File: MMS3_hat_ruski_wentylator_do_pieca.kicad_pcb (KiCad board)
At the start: 2 copper layers, 100 x 50 mm, 72 parts, among them J1 Chainbus in, J2 Chainbus Out, J3 Conn_01x04_Pin, J4 AMASS XT60 Male, J5 AMASS XT60 Female, J6 Conn_01x04_Socket, J7 Program, J9 Conn_01x06_Socket, Q1 PMOS, Q10 AO3401A, Q11 MMBT5401 200-300, Q12 MMBT5551 200-300, Q9 MMBT5551 200-300, U1 SN74CB3Q3245PWR, U2 M24C64, U3 XL6019E1, U4 AMS1117, U5 CH32V003FxPx, U6 MCP4161-502E/SN, X2 X322525MOB4SI

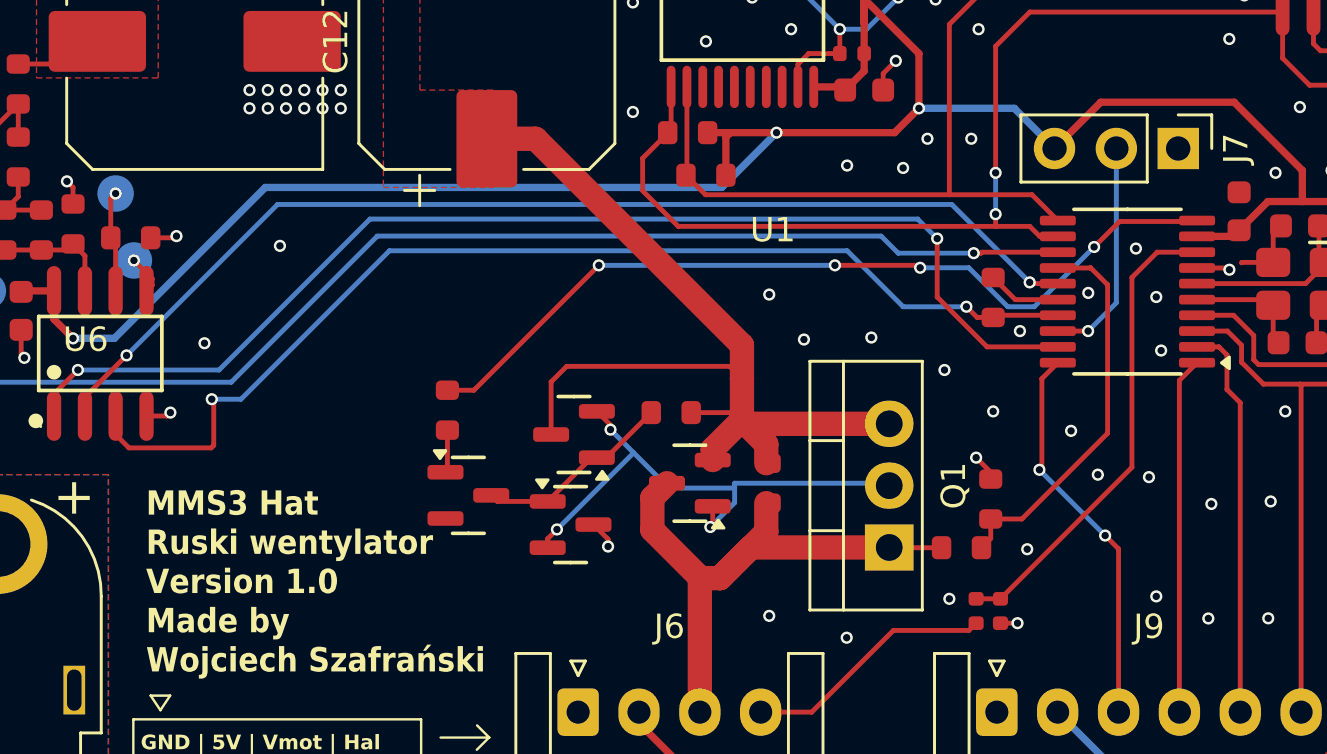
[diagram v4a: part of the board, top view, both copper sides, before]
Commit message: BREAKING: updated CH32v003 programming pinout
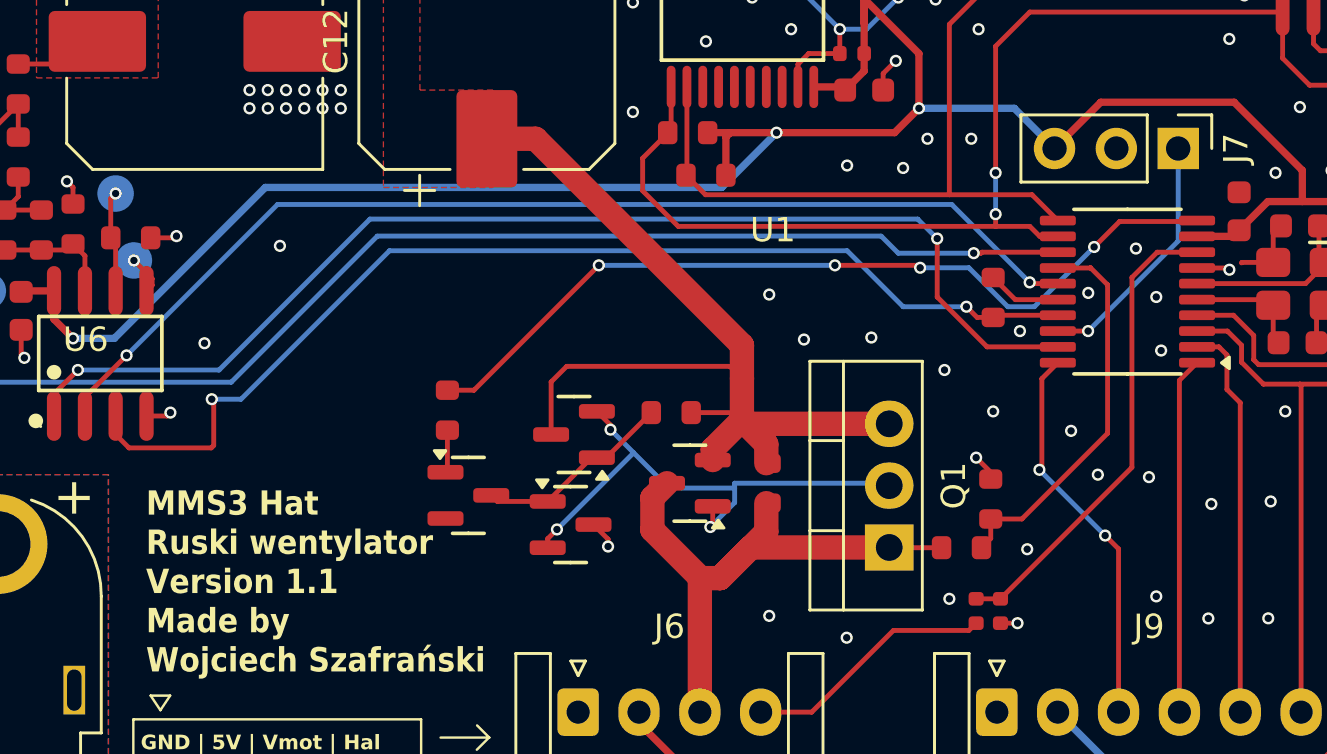
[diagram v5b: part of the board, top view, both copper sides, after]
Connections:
- J7 pad 1: GND -> /CH32V003/SWIO
- J7 pad 2: /CH32V003/SWIO -> GND
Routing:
- net /CH32V003/SWIO: track 9.22 -> 10.3 mm
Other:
- board text added: "MMS3 Hat Ruski wentylator Version 1.1 Made by Wojciech Szafrański"
- board text removed: "MMS3 Hat Ruski wentylator Version 1.0 Made by Wojciech Szafrański"
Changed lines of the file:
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@@
 	(paper "A4")
 	(title_block
-		(title "MMS3 Hat Template (Change Me :3)")
-		(date "2137-02-25")
-		(rev "R0")
+		(title "MMS3 Hat Ruski Wentylator Do Pieca")
+		(date "2026-06-08")
+		(rev "1.1")
 		(comment 1 "Made by Wojciech Szafrański")
 		(comment 2 "Designed in poland")
@@
 			(layers "*.Cu" "*.Mask")
 			(remove_unused_layers no)
-			(net "GND")
+			(net "/CH32V003/SWIO")
 			(pinfunction "Pin_1_1")
 			(pintype "passive")
@@
 			(layers "*.Cu" "*.Mask")
 			(remove_unused_layers no)
-			(net "/CH32V003/SWIO")
+			(net "GND")
 			(pinfunction "Pin_2_2")
 			(pintype "passive")
@@
 			)
 		)
-		(property "KiLib_Generator" "package/TO_SOT/THT"
-			(at 0 0 90)
-			(layer "F.SilkS")
-			(hide yes)
-			(effects
-				(font
-					(size 1 1)
-					(thickness 0.15)
-				)
-			)
-		)
 		(property "Sim.Device" "PMOS"
 			(at 0 0 90)
@@
 		)
 	)
-	(gr_text "MMS3 Hat\nRuski wentylator\nVersion 1.0\nMade by\nWojciech Szafrański"
+	(gr_text "MMS3 Hat\nRuski wentylator\nVersion 1.1\nMade by\nWojciech Szafrański"
 		(at 120 129.7 0)
 		(layer "F.SilkS")
@@
 	)
 	(segment
-		(start 159.86 111.9)
-		(end 159.86 118.24)
+		(start 158.7 119.4)
+		(end 162.4 115.7)
 		(width 0.2)
 		(layer "B.Cu")
@@
 	)
 	(segment
-		(start 159.86 118.24)
-		(end 158.7 119.4)
+		(start 162.4 115.7)
+		(end 162.4 111.9)
 		(width 0.2)
 		(layer "B.Cu")
